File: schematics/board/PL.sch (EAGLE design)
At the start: 25 parts, among them IC2 STM32F103C8T, Q5 8MHz

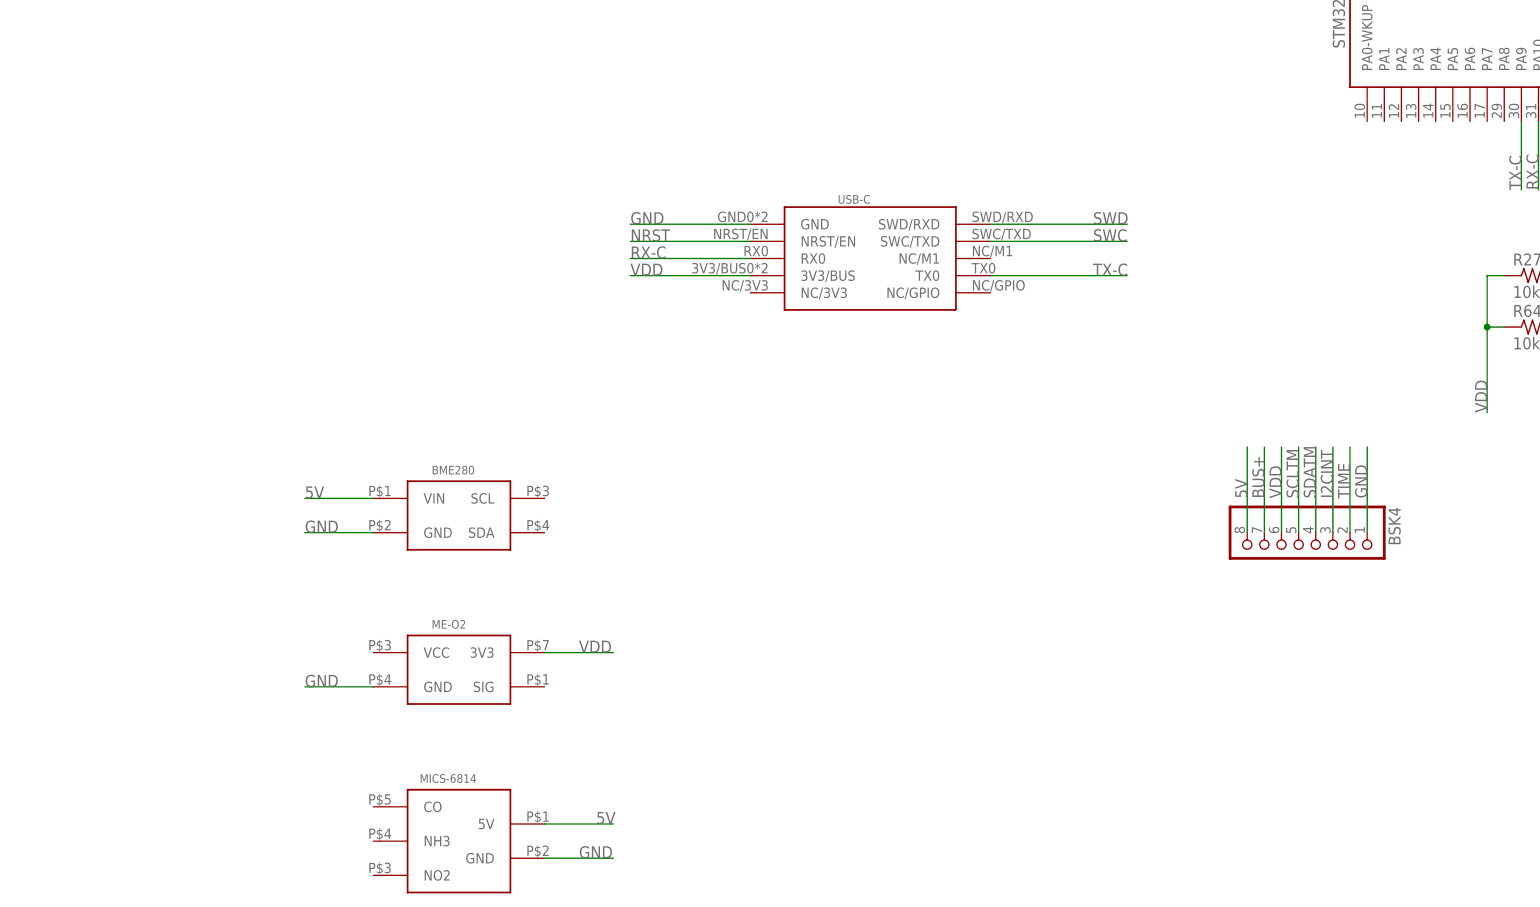
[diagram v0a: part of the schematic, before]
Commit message: Разработана схема подключения датчиков полезной нагрузки. Closes #18
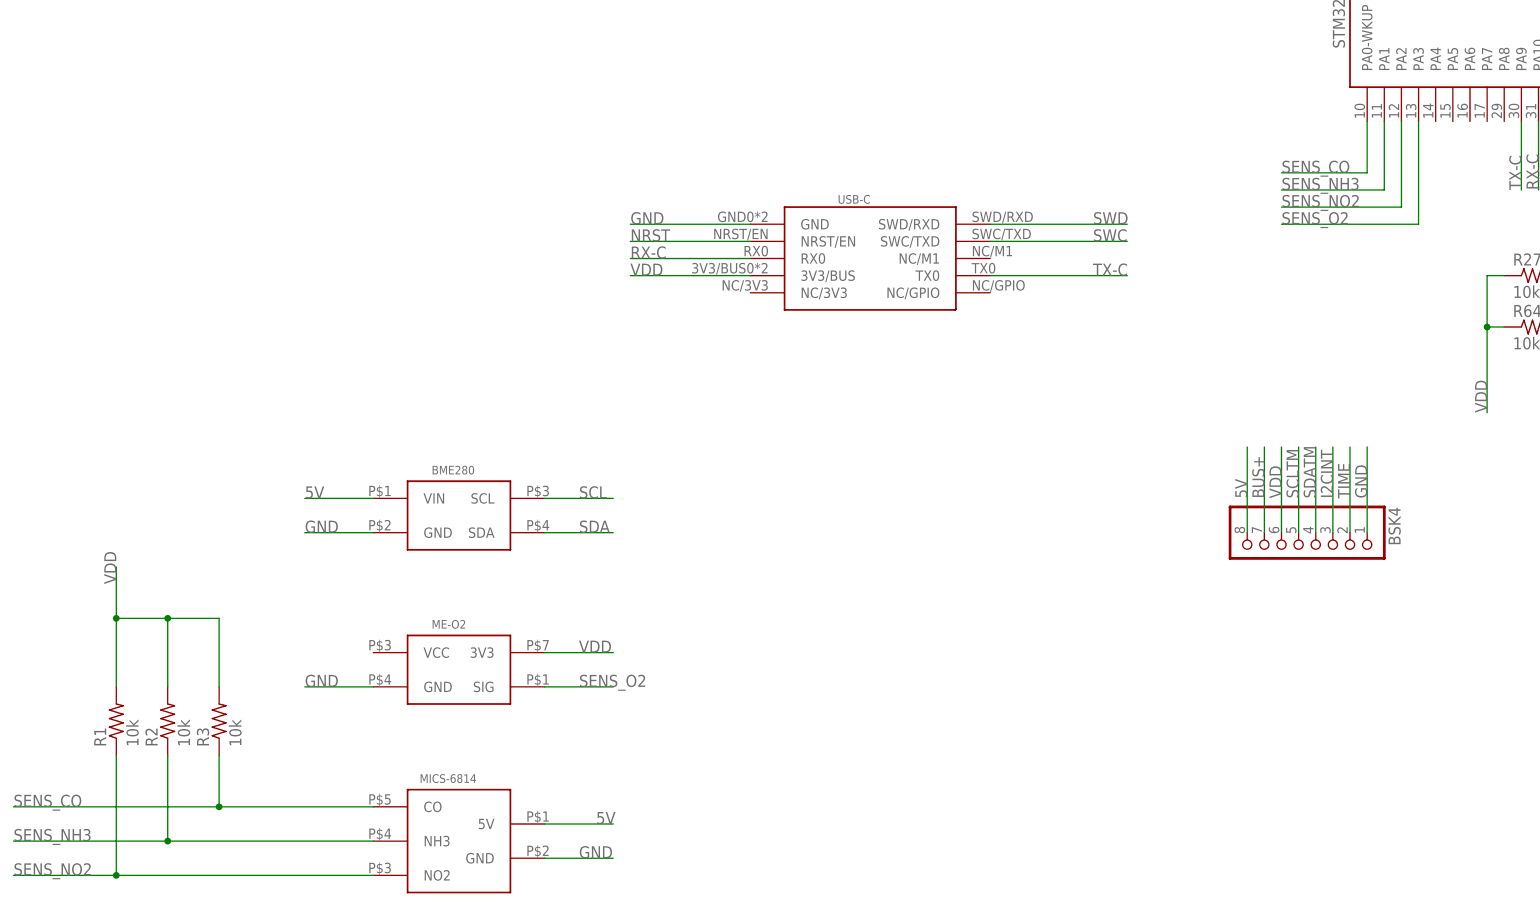
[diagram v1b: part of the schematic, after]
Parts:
- added R1, R2, R3: 10k, resistor:R-US_R0603
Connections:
- new net SENS_CO: IC2.PA0-WKUP, MICS-6814.CO, R3.1
- new net SENS_NH3: IC2.PA1, MICS-6814.NH3, R2.1
- new net SENS_NO2: IC2.PA2, MICS-6814.NO2, R1.1
- new net SENS_O2: IC2.PA3, ME-O2.SIG
- net SCL: now also BME280.SCL
- net SDA: now also BME280.SDA
- net VDD: now also R1.2, R2.2, R3.2
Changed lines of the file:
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@@
 <?xml version="1.0" encoding="utf-8"?>
 <!DOCTYPE eagle SYSTEM "eagle.dtd">
-<eagle version="9.4.2">
+<eagle version="9.6.0">
 <drawing>
 <settings>
@@
 <part name="ME-O2" library="CanCubeSat" deviceset="ME-O2" device=""/>
 <part name="MICS-6814" library="CanCubeSat" deviceset="MICS-6814" device=""/>
+<part name="R1" library="resistor" library_urn="urn:adsk.eagle:library:348" deviceset="R-US_" device="R0603" package3d_urn="urn:adsk.eagle:package:23555/3" value="10k"/>
+<part name="R2" library="resistor" library_urn="urn:adsk.eagle:library:348" deviceset="R-US_" device="R0603" package3d_urn="urn:adsk.eagle:package:23555/3" value="10k"/>
+<part name="R3" library="resistor" library_urn="urn:adsk.eagle:library:348" deviceset="R-US_" device="R0603" package3d_urn="urn:adsk.eagle:package:23555/3" value="10k"/>
 </parts>
 <sheets>
@@
 <instance part="MICS-6814" gate="G$1" x="-48.26" y="-17.78" smashed="yes">
 <attribute name="NAME" x="-54.102" y="-9.144" size="1.27" layer="95"/>
+</instance>
+<instance part="R1" gate="G$1" x="-99.06" y="0" smashed="yes" rot="R90">
+<attribute name="NAME" x="-100.5586" y="-3.81" size="1.778" layer="95" rot="R90"/>
+<attribute name="VALUE" x="-95.758" y="-3.81" size="1.778" layer="96" rot="R90"/>
+</instance>
+<instance part="R2" gate="G$1" x="-91.44" y="0" smashed="yes" rot="R90">
+<attribute name="NAME" x="-92.9386" y="-3.81" size="1.778" layer="95" rot="R90"/>
+<attribute name="VALUE" x="-88.138" y="-3.81" size="1.778" layer="96" rot="R90"/>
+</instance>
+<instance part="R3" gate="G$1" x="-83.82" y="0" smashed="yes" rot="R90">
+<attribute name="NAME" x="-85.3186" y="-3.81" size="1.778" layer="95" rot="R90"/>
+<attribute name="VALUE" x="-80.518" y="-3.81" size="1.778" layer="96" rot="R90"/>
 </instance>
 </instances>
@@
 <pinref part="IC2" gate="MCU" pin="PB10"/>
 </segment>
+<segment>
+<pinref part="BME280" gate="G$1" pin="SCL"/>
+<wire x1="-35.56" y1="33.02" x2="-25.4" y2="33.02" width="0.1524" layer="91"/>
+<label x="-30.48" y="33.02" size="1.778" layer="95"/>
+</segment>
 </net>
 <net name="SDA" class="0">
@@
 <pinref part="R102" gate="G$1" pin="2"/>
 <pinref part="IC2" gate="MCU" pin="PB11"/>
+</segment>
+<segment>
+<pinref part="BME280" gate="G$1" pin="SDA"/>
+<wire x1="-35.56" y1="27.94" x2="-25.4" y2="27.94" width="0.1524" layer="91"/>
+<label x="-30.48" y="27.94" size="1.778" layer="95"/>
 </segment>
 </net>
@@
 <label x="-30.48" y="10.16" size="1.778" layer="95"/>
 </segment>
+<segment>
+<wire x1="-99.06" y1="15.24" x2="-99.06" y2="22.86" width="0.1524" layer="91"/>
+<wire x1="-99.06" y1="15.24" x2="-91.44" y2="15.24" width="0.1524" layer="91"/>
+<wire x1="-91.44" y1="15.24" x2="-91.44" y2="5.08" width="0.1524" layer="91"/>
+<pinref part="R2" gate="G$1" pin="2"/>
+<pinref part="R3" gate="G$1" pin="2"/>
+<wire x1="-91.44" y1="15.24" x2="-83.82" y2="15.24" width="0.1524" layer="91"/>
+<wire x1="-83.82" y1="15.24" x2="-83.82" y2="5.08" width="0.1524" layer="91"/>
+<junction x="-91.44" y="15.24"/>
+<pinref part="R1" gate="G$1" pin="2"/>
+<wire x1="-99.06" y1="15.24" x2="-99.06" y2="5.08" width="0.1524" layer="91"/>
+<junction x="-99.06" y="15.24"/>
+<label x="-99.06" y="20.32" size="1.778" layer="95" rot="R90"/>
+</segment>
 </net>
 <net name="N$133" class="0">
@@
 </segment>
 </net>
+<net name="SENS_CO" class="0">
+<segment>
+<pinref part="MICS-6814" gate="G$1" pin="CO"/>
+<pinref part="R3" gate="G$1" pin="1"/>
+<wire x1="-83.82" y1="-5.08" x2="-83.82" y2="-12.7" width="0.1524" layer="91"/>
+<wire x1="-83.82" y1="-12.7" x2="-60.96" y2="-12.7" width="0.1524" layer="91"/>
+<label x="-114.3" y="-12.7" size="1.778" layer="95"/>
+<wire x1="-83.82" y1="-12.7" x2="-114.3" y2="-12.7" width="0.1524" layer="91"/>
+<junction x="-83.82" y="-12.7"/>
+</segment>
+<segment>
+<pinref part="IC2" gate="MCU" pin="PA0-WKUP"/>
+<wire x1="86.36" y1="88.9" x2="86.36" y2="81.28" width="0.1524" layer="91"/>
+<wire x1="86.36" y1="81.28" x2="73.66" y2="81.28" width="0.1524" layer="91"/>
+<label x="73.66" y="81.28" size="1.778" layer="95"/>
+</segment>
+</net>
+<net name="SENS_NH3" class="0">
+<segment>
+<pinref part="MICS-6814" gate="G$1" pin="NH3"/>
+<pinref part="R2" gate="G$1" pin="1"/>
+<wire x1="-60.96" y1="-17.78" x2="-91.44" y2="-17.78" width="0.1524" layer="91"/>
+<wire x1="-91.44" y1="-17.78" x2="-91.44" y2="-5.08" width="0.1524" layer="91"/>
+<label x="-114.3" y="-17.78" size="1.778" layer="95"/>
+<wire x1="-91.44" y1="-17.78" x2="-114.3" y2="-17.78" width="0.1524" layer="91"/>
+<junction x="-91.44" y="-17.78"/>
+</segment>
+<segment>
+<pinref part="IC2" gate="MCU" pin="PA1"/>
+<wire x1="88.9" y1="88.9" x2="88.9" y2="78.74" width="0.1524" layer="91"/>
+<wire x1="88.9" y1="78.74" x2="73.66" y2="78.74" width="0.1524" layer="91"/>
+<label x="73.66" y="78.74" size="1.778" layer="95"/>
+</segment>
+</net>
+<net name="SENS_NO2" class="0">
+<segment>
+<pinref part="MICS-6814" gate="G$1" pin="NO2"/>
+<pinref part="R1" gate="G$1" pin="1"/>
+<wire x1="-60.96" y1="-22.86" x2="-99.06" y2="-22.86" width="0.1524" layer="91"/>
+<wire x1="-99.06" y1="-22.86" x2="-99.06" y2="-5.08" width="0.1524" layer="91"/>
+<label x="-114.3" y="-22.86" size="1.778" layer="95"/>
+<wire x1="-99.06" y1="-22.86" x2="-114.3" y2="-22.86" width="0.1524" layer="91"/>
+<junction x="-99.06" y="-22.86"/>
+</segment>
+<segment>
+<pinref part="IC2" gate="MCU" pin="PA2"/>
+<wire x1="91.44" y1="88.9" x2="91.44" y2="76.2" width="0.1524" layer="91"/>
+<wire x1="91.44" y1="76.2" x2="73.66" y2="76.2" width="0.1524" layer="91"/>
+<label x="73.66" y="76.2" size="1.778" layer="95"/>
+</segment>
+</net>
+<net name="SENS_O2" class="0">
+<segment>
+<pinref part="IC2" gate="MCU" pin="PA3"/>
+<wire x1="93.98" y1="88.9" x2="93.98" y2="73.66" width="0.1524" layer="91"/>
+<wire x1="93.98" y1="73.66" x2="73.66" y2="73.66" width="0.1524" layer="91"/>
+<label x="73.66" y="73.66" size="1.778" layer="95"/>
+</segment>
+<segment>
+<pinref part="ME-O2" gate="G$1" pin="SIG"/>
+<wire x1="-35.56" y1="5.08" x2="-25.4" y2="5.08" width="0.1524" layer="91"/>
+<label x="-30.48" y="5.08" size="1.778" layer="95"/>
+</segment>
+</net>

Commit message: Исправлена плата TESTPL
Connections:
- net VDD: now also IC2.VBAT
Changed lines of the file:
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@@
 <?xml version="1.0" encoding="utf-8"?>
 <!DOCTYPE eagle SYSTEM "eagle.dtd">
-<eagle version="9.6.0">
+<eagle version="9.4.2">
 <drawing>
 <settings>
-<setting alwaysvectorfont="no"/>
+<setting alwaysvectorfont="yes"/>
 <setting verticaltext="up"/>
 </settings>
@@
 <label x="96.52" y="137.16" size="1.778" layer="95" rot="R90"/>
 <pinref part="IC2" gate="MCU" pin="VDDA"/>
-</segment>
-<segment>
+<pinref part="IC2" gate="MCU" pin="VBAT"/>
+<wire x1="99.06" y1="134.62" x2="96.52" y2="134.62" width="0.1524" layer="91"/>
+<junction x="96.52" y="134.62"/>
+</segment>
+<segment>

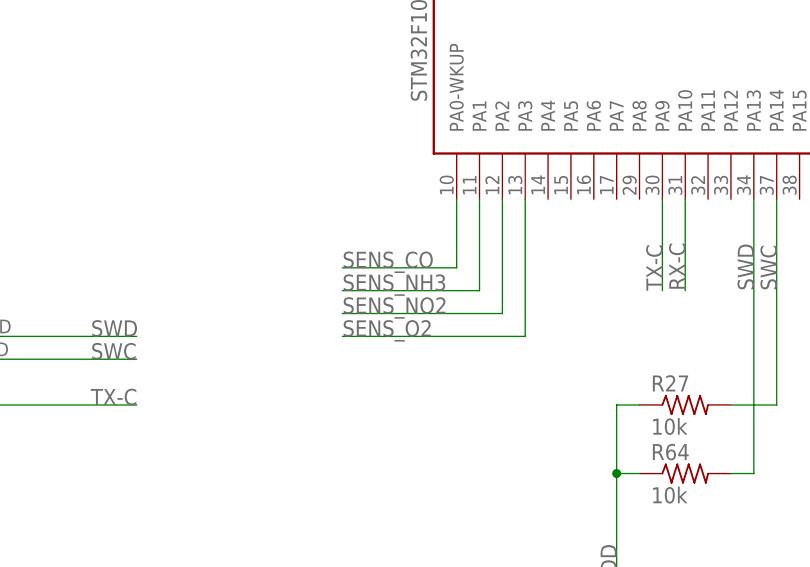
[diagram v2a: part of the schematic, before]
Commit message: Разведена плата PL
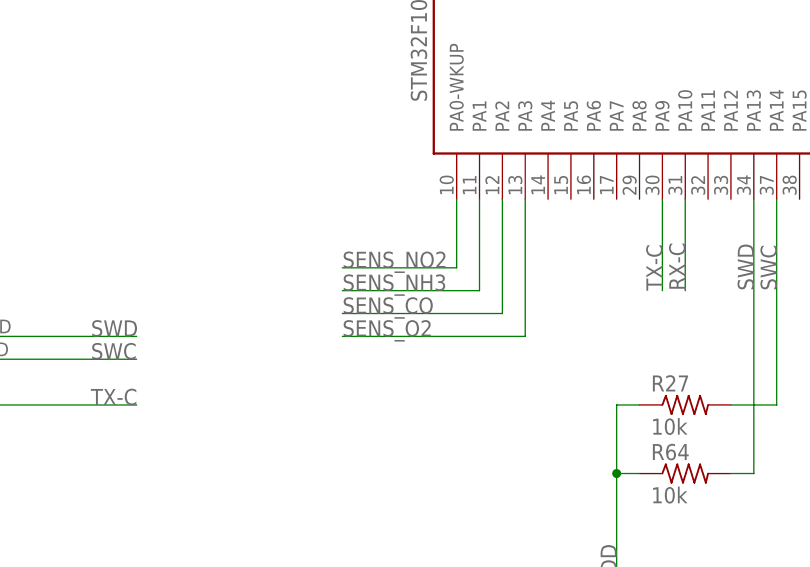
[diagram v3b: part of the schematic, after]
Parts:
- renumbered U$23 to USB-C
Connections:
- net SENS_CO: now also IC2.PA2; no longer IC2.PA0-WKUP
- net SENS_NO2: now also IC2.PA0-WKUP; no longer IC2.PA2
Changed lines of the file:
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@@
 <part name="R25" library="resistor" library_urn="urn:adsk.eagle:library:348" deviceset="R-US_" device="R0603" package3d_urn="urn:adsk.eagle:package:23555/3" value="5k1"/>
 <part name="R26" library="resistor" library_urn="urn:adsk.eagle:library:348" deviceset="R-US_" device="R0603" package3d_urn="urn:adsk.eagle:package:23555/3" value="5k1"/>
-<part name="U$23" library="CanCubeSat" deviceset="USB-C" device=""/>
+<part name="USB-C" library="CanCubeSat" deviceset="USB-C" device=""/>
 <part name="BME280" library="CanCubeSat" deviceset="BME280" device=""/>
 <part name="ME-O2" library="CanCubeSat" deviceset="ME-O2" device=""/>
@@
 <attribute name="VALUE" x="155.702" y="57.15" size="1.778" layer="96" rot="R90"/>
 </instance>
-<instance part="U$23" gate="G$1" x="12.7" y="68.58" smashed="yes"/>
+<instance part="USB-C" gate="G$1" x="12.7" y="68.58" smashed="yes"/>
 <instance part="BME280" gate="G$1" x="-48.26" y="30.48" smashed="yes">
 <attribute name="NAME" x="-52.324" y="36.576" size="1.27" layer="95"/>
@@
 <wire x1="-5.08" y1="73.66" x2="-22.86" y2="73.66" width="0.1524" layer="91"/>
 <label x="-22.86" y="73.66" size="1.778" layer="95"/>
-<pinref part="U$23" gate="G$1" pin="GND"/>
+<pinref part="USB-C" gate="G$1" pin="GND"/>
 </segment>
 <segment>
@@
 <wire x1="-5.08" y1="66.04" x2="-22.86" y2="66.04" width="0.1524" layer="91"/>
 <label x="-22.86" y="66.04" size="1.778" layer="95"/>
-<pinref part="U$23" gate="G$1" pin="3V3/BUS"/>
+<pinref part="USB-C" gate="G$1" pin="3V3/BUS"/>
 </segment>
 <segment>
@@
 <label x="45.72" y="71.12" size="1.778" layer="95"/>
 <wire x1="30.48" y1="71.12" x2="50.8" y2="71.12" width="0.1524" layer="91"/>
-<pinref part="U$23" gate="G$1" pin="SWC/TXD"/>
+<pinref part="USB-C" gate="G$1" pin="SWC/TXD"/>
 </segment>
 </net>
@@
 <wire x1="30.48" y1="73.66" x2="50.8" y2="73.66" width="0.1524" layer="91"/>
 <label x="45.72" y="73.66" size="1.778" layer="95"/>
-<pinref part="U$23" gate="G$1" pin="SWD/RXD"/>
+<pinref part="USB-C" gate="G$1" pin="SWD/RXD"/>
 </segment>
 </net>
@@
 <wire x1="50.8" y1="66.04" x2="30.48" y2="66.04" width="0.1524" layer="91"/>
 <label x="45.72" y="66.04" size="1.778" layer="95"/>
-<pinref part="U$23" gate="G$1" pin="TX0"/>
+<pinref part="USB-C" gate="G$1" pin="TX0"/>
 </segment>
 </net>
@@
 <wire x1="-22.86" y1="68.58" x2="-5.08" y2="68.58" width="0.1524" layer="91"/>
 <label x="-22.86" y="68.58" size="1.778" layer="95"/>
-<pinref part="U$23" gate="G$1" pin="RX0"/>
+<pinref part="USB-C" gate="G$1" pin="RX0"/>
 </segment>
 </net>
@@
 <wire x1="-22.86" y1="71.12" x2="-5.08" y2="71.12" width="0.1524" layer="91"/>
 <label x="-22.86" y="71.12" size="1.778" layer="95"/>
-<pinref part="U$23" gate="G$1" pin="NRST/EN"/>
+<pinref part="USB-C" gate="G$1" pin="NRST/EN"/>
 </segment>
 </net>
@@
 </segment>
 <segment>
-<pinref part="IC2" gate="MCU" pin="PA0-WKUP"/>
-<wire x1="86.36" y1="88.9" x2="86.36" y2="81.28" width="0.1524" layer="91"/>
-<wire x1="86.36" y1="81.28" x2="73.66" y2="81.28" width="0.1524" layer="91"/>
-<label x="73.66" y="81.28" size="1.778" layer="95"/>
+<pinref part="IC2" gate="MCU" pin="PA2"/>
+<wire x1="91.44" y1="88.9" x2="91.44" y2="76.2" width="0.1524" layer="91"/>
+<wire x1="91.44" y1="76.2" x2="73.66" y2="76.2" width="0.1524" layer="91"/>
+<label x="73.66" y="76.2" size="1.778" layer="95"/>
 </segment>
 </net>
@@
 </segment>
 <segment>
-<pinref part="IC2" gate="MCU" pin="PA2"/>
-<wire x1="91.44" y1="88.9" x2="91.44" y2="76.2" width="0.1524" layer="91"/>
-<wire x1="91.44" y1="76.2" x2="73.66" y2="76.2" width="0.1524" layer="91"/>
-<label x="73.66" y="76.2" size="1.778" layer="95"/>
-</segment>
-</net>
+<pinref part="IC2" gate="MCU" pin="PA0-WKUP"/>
+<wire x1="86.36" y1="88.9" x2="86.36" y2="81.28" width="0.1524" layer="91"/>
+<wire x1="86.36" y1="81.28" x2="73.66" y2="81.28" width="0.1524" layer="91"/>
+<label x="73.66" y="81.28" size="1.778" layer="95"/>
+</segment>
+</net>
